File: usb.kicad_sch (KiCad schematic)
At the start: 12 parts, among them IC3 TPD8S300RUKR, IC9 TPS259571DSGR, J4 UJ20-C-V-SMT-TR-68

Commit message: finished usb connection ciruits
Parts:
- added R17, R18, R19, R20: 5k1 50mW, Resistor_SMD:R_0201_0603Metric, symbol Device:R_Small
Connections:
- net GND: now also IC3.6 (RPD_G2), IC3.7 (RPD_G1), R17.2, R18.2, R19.2, R20.2
- net at IC3.4 (C_CC1), J4.A5 (CC1): now also R20.1
- net at IC3.5 (C_CC2), J4.B5 (CC2): now also R19.1
- net CC1: no longer names the net of IC3.12 (CC1)
- net CC1: now also R18.1; no longer IC3.7 (RPD_G1)
- net CC2: no longer names the net of IC3.11 (CC2)
- net CC2: now also R17.1; no longer IC3.6 (RPD_G2)
- net SBU_N: no longer names the net of IC3.14 (SBU2)
- net SBU_P: no longer names the net of IC3.15 (SBU1)
- net VCHARGE renamed VUSB
- no-connect marks 0 -> 2
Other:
- note added: "optional termination"
- note removed: "Battery Connector"
- moved on the sheet: C8, IC3, R3

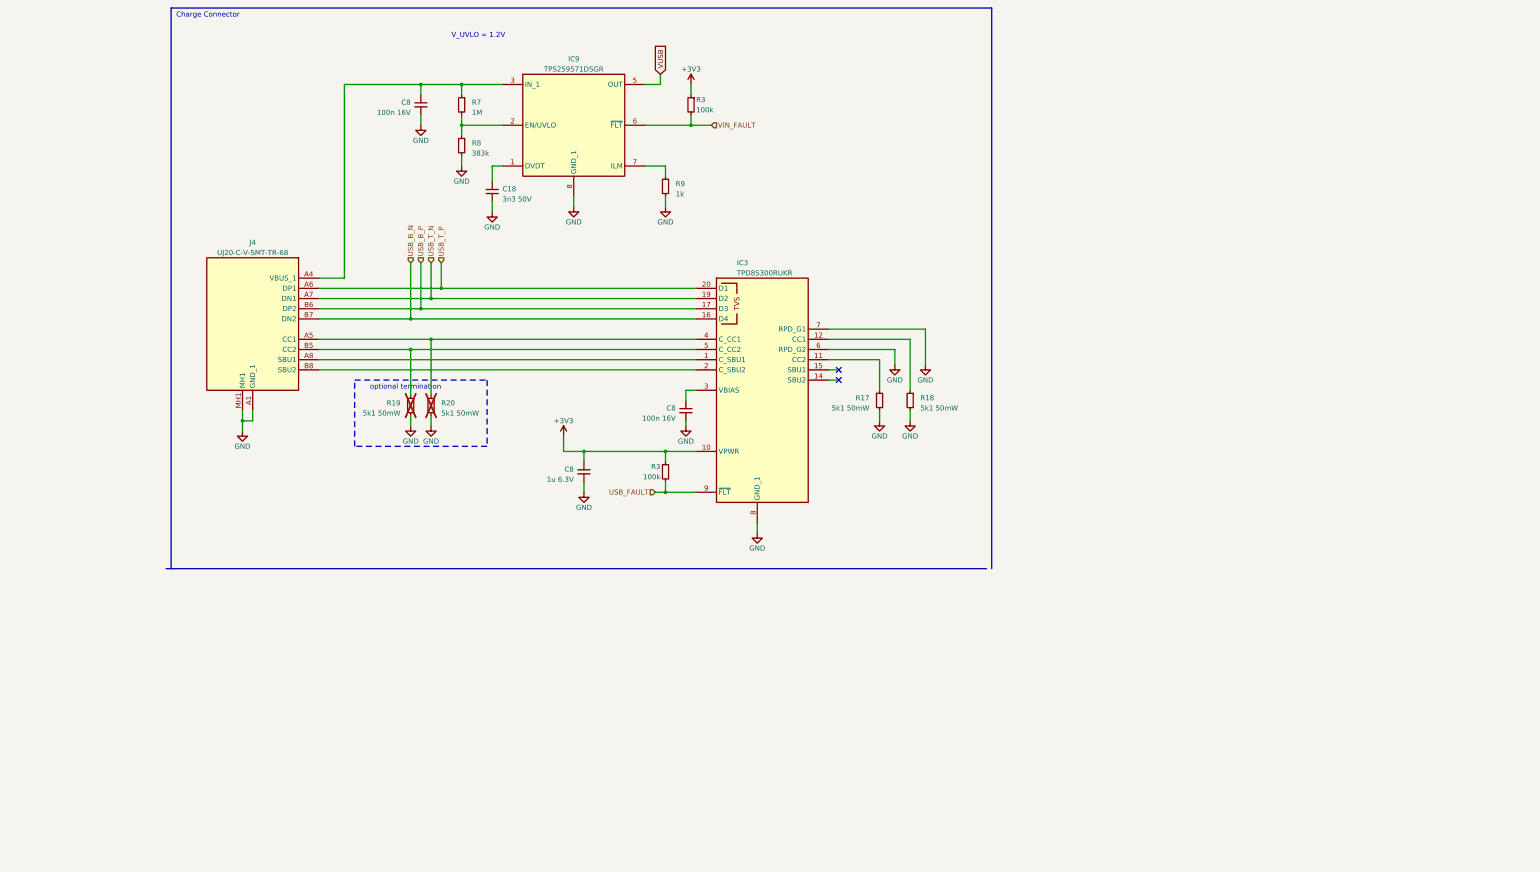
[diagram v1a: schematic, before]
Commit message: switched to other charge + protection IC
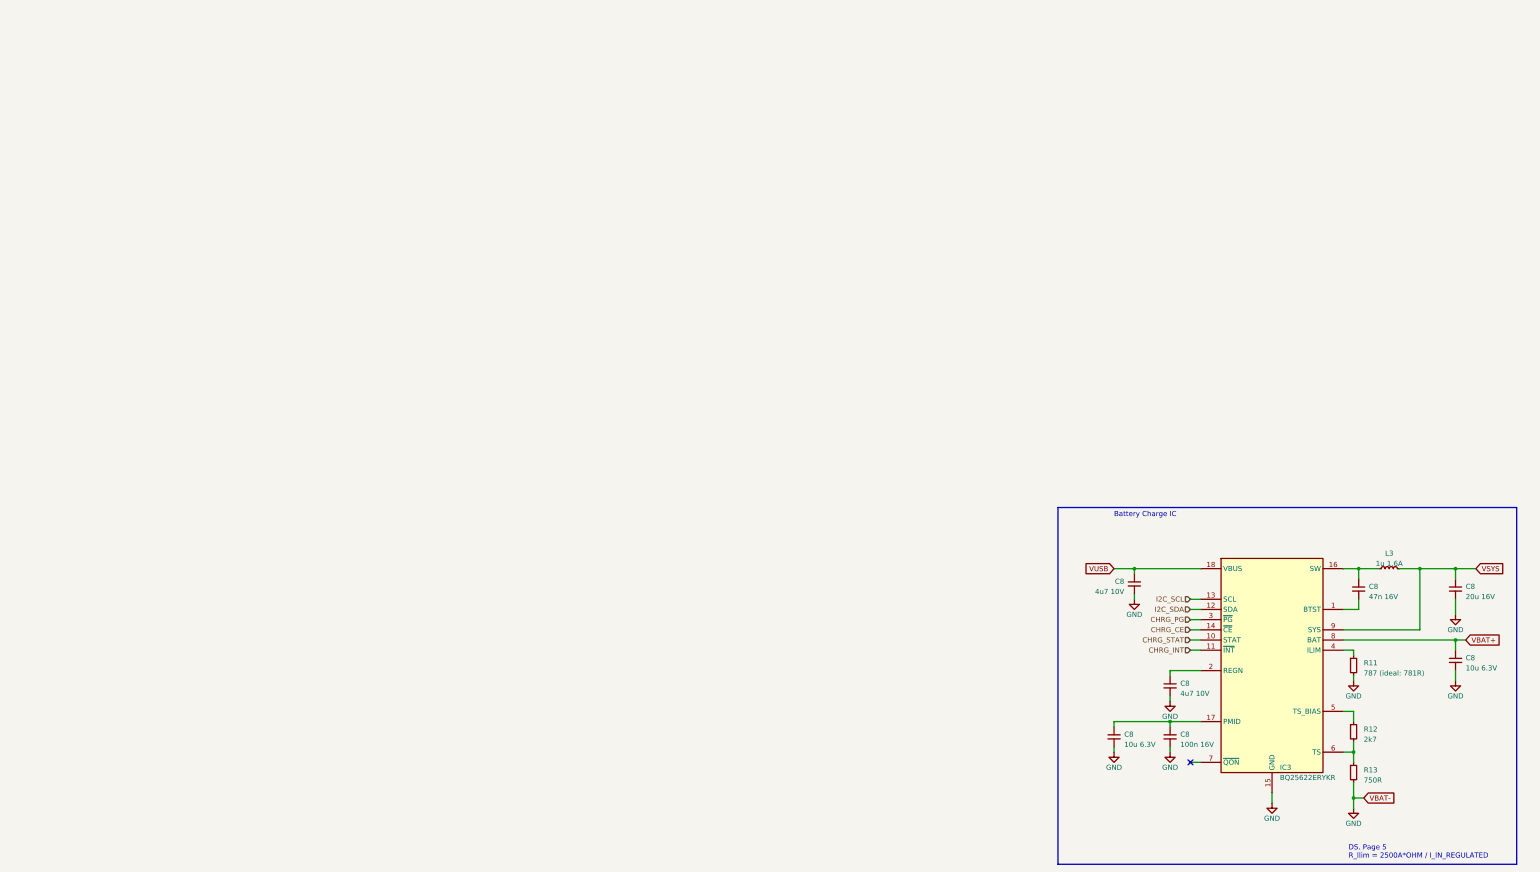
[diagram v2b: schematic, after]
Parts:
- removed C18: 3n3 50V, Capacitor_SMD:C_0402_1005Metric, symbol Device:C_Small
- removed C8: 1u 6.3V, Capacitor_SMD:C_0201_0603Metric, symbol Device:C_Small
- removed C8 (x2): 100n 16V, Capacitor_SMD:C_0402_1005Metric, symbol Device:C_Small
- removed IC3: TPD8S300RUKR, ARMband:QFN40P300X300X80-21N-D, symbol ARMband:TPD8S300RUKR
- removed IC9: TPS259571DSGR, SON50P200X200X80-9N, symbol LibraryLoader:TPS259571DSGR
- removed J4: UJ20-C-V-SMT-TR-68, ARMband:UJ20CVSMTTR68, symbol ARMband:UJ20-C-V-SMT-TR-68
- removed R17, R18, R19, R20: 5k1 50mW, Resistor_SMD:R_0201_0603Metric, symbol Device:R_Small
- removed R3 (x2): 100k, Resistor_SMD:R_0201_0603Metric_Pad0.64x0.40mm_HandSolder, symbol Device:R_Small
- removed R7: 1M, Resistor_SMD:R_0201_0603Metric, symbol Device:R_Small
- removed R8: 383k, Resistor_SMD:R_0201_0603Metric, symbol Device:R_Small
- removed R9: 1k, Resistor_SMD:R_0201_0603Metric, symbol Device:R_Small
- added C8: 100n 16V, Capacitor_SMD:C_0402_1005Metric, symbol Device:C_Small
- added C8 (x2): 10u 6.3V, Capacitor_SMD:C_0402_1005Metric, symbol Device:C_Small
- added C8 (x2): 4u7 10V, Capacitor_SMD:C_0402_1005Metric, symbol Device:C_Small
- added C8: 47n 16V, Capacitor_SMD:C_0201_0603Metric, symbol Device:C_Small
- added C8: 20u 16V, ARMband:C_0704, symbol Device:C_Small
- added IC3: BQ25622ERYKR, ARMband:BQ25620RYKR, symbol ARMband:BQ25622ERYKR
- added L3: 1u 1.6A, Inductor_SMD:L_0603_1608Metric, symbol Device:L_Small
- added R11: 787 (ideal: 781R), Resistor_SMD:R_0201_0603Metric, symbol Device:R_Small
- added R12: 2k7, symbol Device:R_Small
- added R13: 750R, symbol Device:R_Small
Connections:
- net GND: now also C8.2, C8.2, C8.2, C8.2, C8.2, C8.2, IC3.15 (GND), R11.2, R13.2
- net VUSB: now also C8.1, IC3.18 (VBUS)
- new net: C8.1, C8.1, IC3.17 (PMID)
- new net: IC3.4 (ILIM), R11.1
- new net: C8.1, IC3.2 (REGN)
- new net: C8.1, IC3.16 (SW), L3.1
- new net: C8.2, IC3.1 (BTST)
- new net: IC3.5 (TS_BIAS), R12.1
- new net: IC3.6 (TS), R12.2, R13.1
- new net CHRG_CE: IC3.14 (~{CE})
- new net CHRG_INT: IC3.11 (~{INT})
- new net CHRG_PG: IC3.3 (~{PG})
- new net CHRG_STAT: IC3.10 (STAT)
- new net I2C_SCL: IC3.13 (SCL)
- new net I2C_SDA: IC3.12 (SDA)
- new net VBAT+: C8.1, IC3.8 (BAT)
- new net VSYS: C8.1, IC3.9 (SYS), L3.2
- no-connect marks 2 -> 1
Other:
- note added: "Battery Charge IC"
- note added: "DS. Page 5 R_Ilim = 2500A*OHM / I_IN_REGULATED"
- note removed: "Charge Connector"
- note removed: "V_UVLO = 1.2V"
- note removed: "optional termination"
